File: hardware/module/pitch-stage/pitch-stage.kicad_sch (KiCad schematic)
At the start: 0 parts

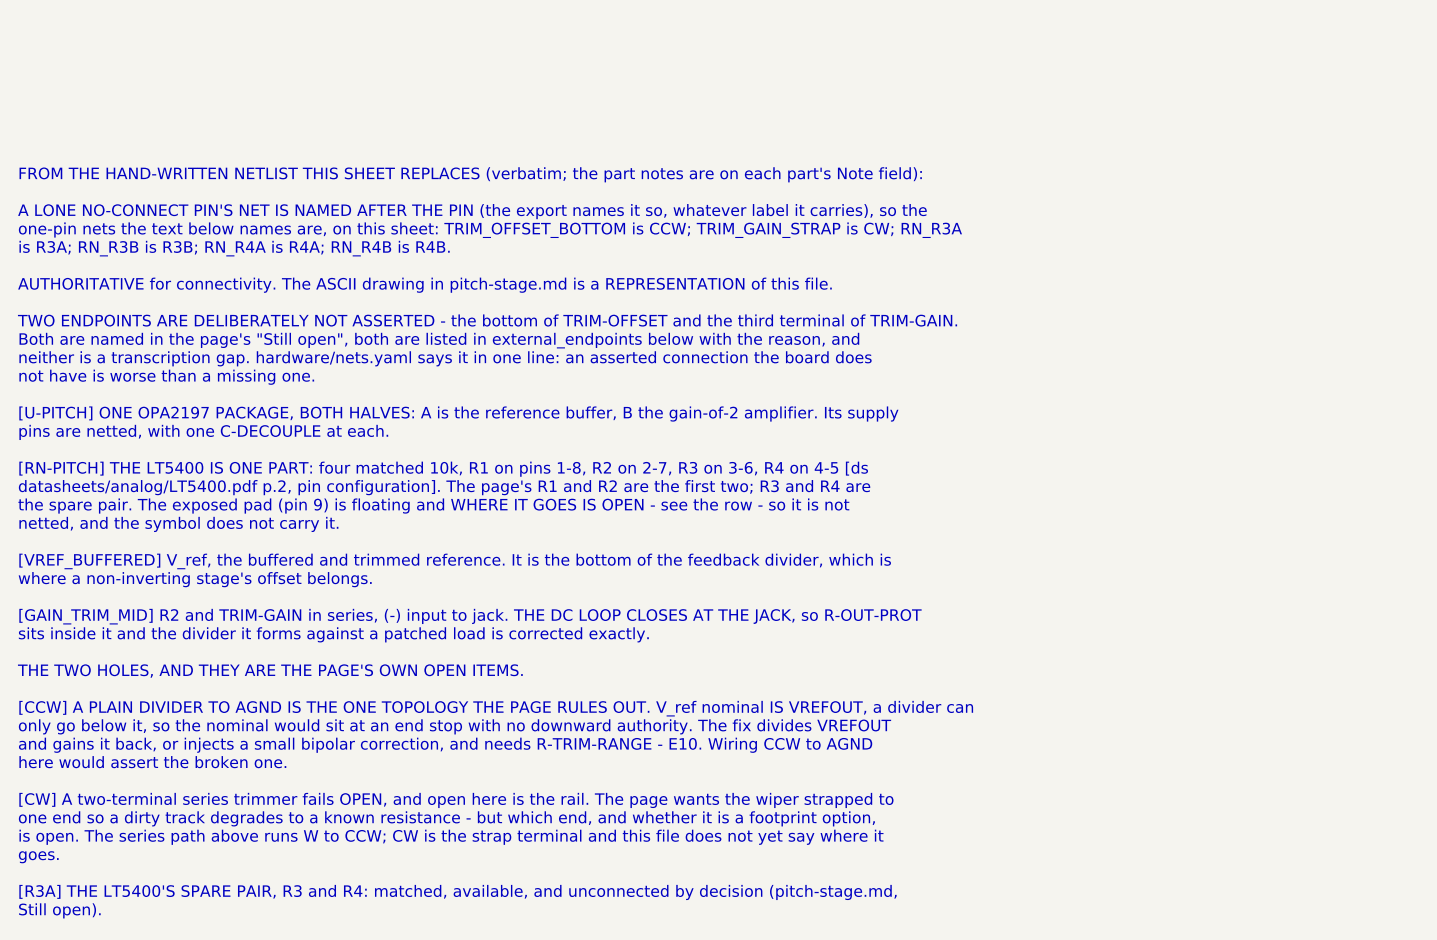
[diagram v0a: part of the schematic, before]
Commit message: Module: D3 turned round; pitch trims made buildable and bipolar; LT5400 pad and order code; breath-zero range resistor
D3 (the -12 V entry diode) was netlisted anode-to-bus, reverse-biased in
normal running (found by the analog sims): cathode to the bus now.
TRIM-OFFSET spans VREFOUT-AGND and injects through R-VREF-INJ against
R-VREF-SER into the follower at gain 1.02 (R-VREF-FB/R-VREF-GND): 2.500 V at
mid-travel, -60/+50 mV. It also holds the 3-state VREFOUT at 0 V while the
DAC's reference is disabled. TRIM-GAIN is centred by R-GAIN-CTR in the R1 leg
(+/-1 %) and its CW end strapped to the wiper. RN-PITCH carries its exposed
pad as pin 9 to AGND_MOD, spares tied down; ordered LT5400BIMS8E-1#PBF.
R-OPAMP-IN is six; R-TRIM-RANGE split into real parts. R-ZERO-TOP gives
TRIM-BREATH-ZERO the 0-1.0 V range its page specifies. Page text follows.

Co-Authored-By: Claude Opus 5.5 <noreply@anthropic.com>
Claude-Session: https://claude.ai/code/session_01LmB4muFXnoLprWX4JzuJ5A
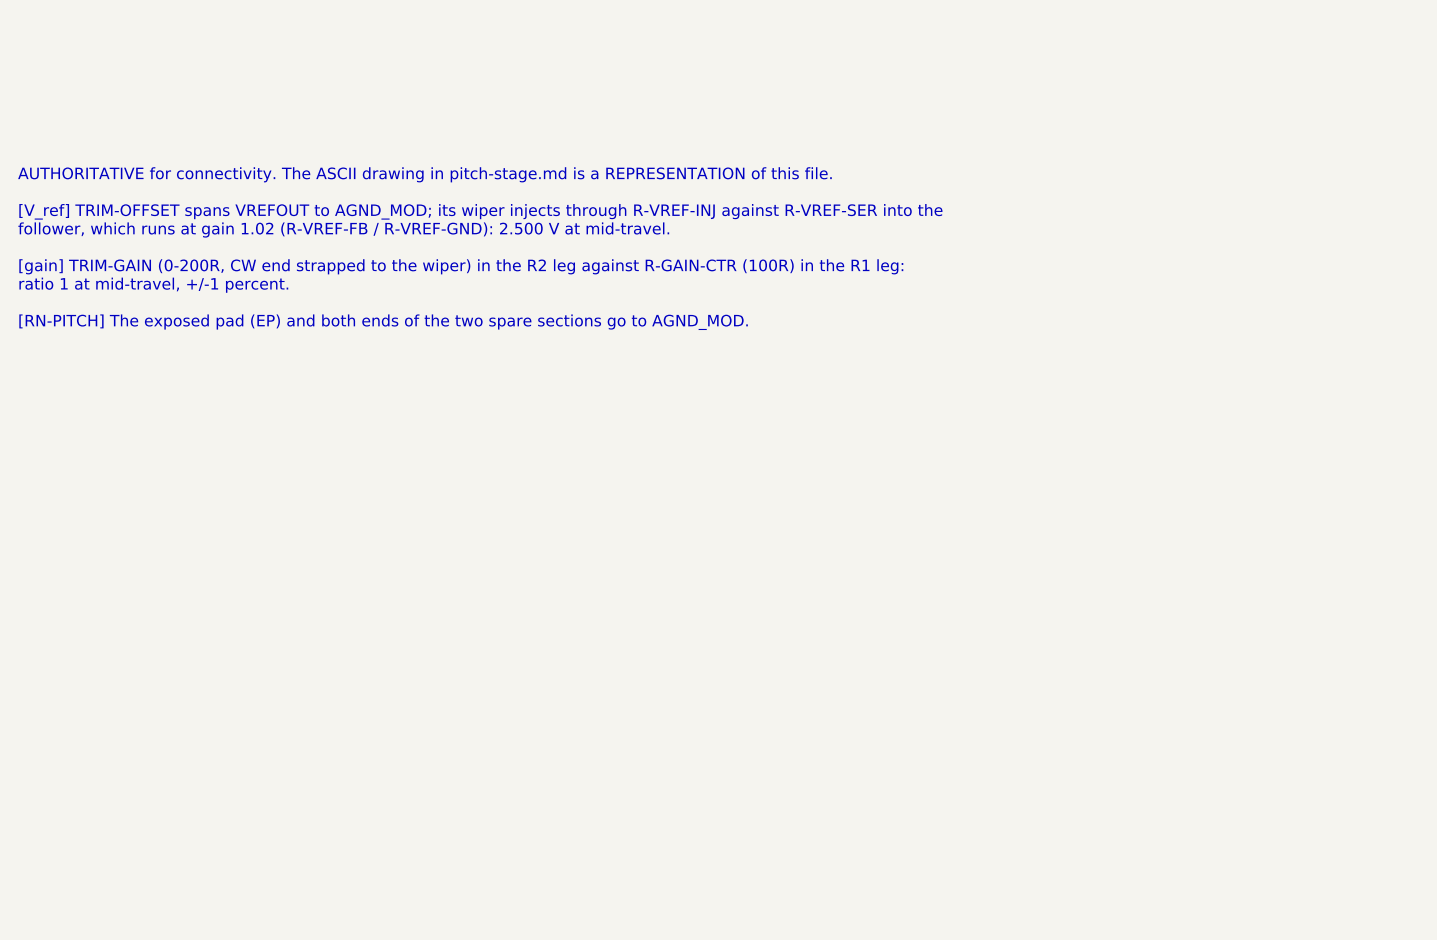
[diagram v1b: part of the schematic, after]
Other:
- note added: "AUTHORITATIVE for connectivity. The ASCII drawing in pitch-stage.md is a REPRESENTATION of this file. [V_ref] TRIM-OFFSET spans VREFOUT to AGND_MOD; its wiper injects through R-VREF-INJ against R-VREF-SER into the follower, which runs at gain 1.02 (R-VREF-FB / R-VREF-GND): 2.500 V at mid-travel. [gain] TRIM-GAIN (0-200R, CW end strapped to the wiper) in the R2 leg against R-GAIN-CTR (100R) in the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"
- note removed: "FROM THE HAND-WRITTEN NETLIST THIS SHEET REPLACES (verbatim; the part notes are on each part's Note field): A LONE NO-CONNECT PIN'S NET IS NAMED AFTER THE PIN (the export names it so, whatever label it carries), so the one-pin nets the text below names are, on this sheet: TRIM_OFFSET_BOTTOM is CCW; TRIM_GAIN_STRAP is CW; RN_R3A is R3A; RN_R3B is R3B; RN_R4A is R4A; RN_R4B is R4B. AUTHORITATIVE fo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"
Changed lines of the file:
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@@
     (property "From" "module/power-entry" (at 269.24 55.88 0) (effects (font (size 1.27 1.27)) hide))
     (property "Figure" "dig-gnd-topology" (at 269.24 55.88 0) (effects (font (size 1.27 1.27)) hide)))
-  (text "FROM THE HAND-WRITTEN NETLIST THIS SHEET REPLACES (verbatim; the part notes are on each part's Note field):\n\nA LONE NO-CONNECT PIN'S NET IS NAMED AFTER THE PIN (the export names it so, whatever label it carries), so the\none-pin nets the text below names are, on this sheet: TRIM_OFFSET_BOTTOM is CCW; TRIM_GAIN_STRAP is CW; RN_R3A\nis R3A; RN_R3B is R3B; RN_R4A is R4A; RN_R4B is R4B.\n\nAUTHORITATIVE for connectivity. The ASCII drawing in pitch-stage.md is a REPRESENTATION of this file.\n\nTWO ENDPOINTS ARE DELIBERATELY NOT ASSERTED - the bottom of TRIM-OFFSET and the third terminal of TRIM-GAIN.\nBoth are named in the page's \"Still open\", both are listed in external_endpoints below with the reason, and\nneither is a transcription gap. hardware/nets.yaml says it in one line: an asserted connection the board does\nnot have is worse than a missing one.\n\n[U-PITCH] ONE OPA2197 PACKAGE, BOTH HALVES: A is the reference buffer, B the gain-of-2 amplifier. Its supply\npins are netted, with one C-DECOUPLE at each.\n\n[RN-PITCH] THE LT5400 IS ONE PART: four matched 10k, R1 on pins 1-8, R2 on 2-7, R3 on 3-6, R4 on 4-5 [ds\ndatasheets/analog/LT5400.pdf p.2, pin configuration]. The page's R1 and R2 are the first two; R3 and R4 are\nthe spare pair. The exposed pad (pin 9) is floating and WHERE IT GOES IS OPEN - see the row - so it is not\nnetted, and the symbol does not carry it.\n\n[VREF_BUFFERED] V_ref, the buffered and trimmed reference. It is the bottom of the feedback divider, which is\nwhere a non-inverting stage's offset belongs.\n\n[GAIN_TRIM_MID] R2 and TRIM-GAIN in series, (-) input to jack. THE DC LOOP CLOSES AT THE JACK, so R-OUT-PROT\nsits inside it and the divider it forms against a patched load is corrected exactly.\n\nTHE TWO HOLES, AND THEY ARE THE PAGE'S OWN OPEN ITEMS.\n\n[CCW] A PLAIN DIVIDER TO AGND IS THE ONE TOPOLOGY THE PAGE RULES OUT. V_ref nominal IS VREFOUT, a divider can\nonly go below it, so the nominal would sit at an end stop with no downward authority. The fix divides VREFOUT\nand gains it back, or injects a small bipolar correction, and needs R-TRIM-RANGE - E10. Wiring CCW to AGND\nhere would assert the broken one.\n\n[CW] A two-terminal series trimmer fails OPEN, and open here is the rail. The page wants the wiper strapped to\none end so a dirty track degrades to a known resistance - but which end, and whether it is a footprint option,\nis open. The series path above runs W to CCW; CW is the strap terminal and this file does not yet say where it\ngoes.\n\n[R3A] THE LT5400'S SPARE PAIR, R3 and R4: matched, available, and unconnected by decision (pitch-stage.md,\nStill open)." (at 40.64 147.32 0) (effects (font (size 1.27 1.27)) (justify left top)))
+  (text "AUTHORITATIVE for connectivity. The ASCII drawing in pitch-stage.md is a REPRESENTATION of this file.\n\n[V_ref] TRIM-OFFSET spans VREFOUT to AGND_MOD; its wiper injects through R-VREF-INJ against R-VREF-SER into the\nfollower, which runs at gain 1.02 (R-VREF-FB / R-VREF-GND): 2.500 V at mid-travel.\n\n[gain] TRIM-GAIN (0-200R, CW end strapped to the wiper) in the R2 leg against R-GAIN-CTR (100R) in the R1 leg:\nratio 1 at mid-travel, +/-1 percent.\n\n[RN-PITCH] The exposed pad (EP) and both ends of the two spare sections go to AGND_MOD." (at 40.64 147.32 0) (effects (font (size 1.27 1.27)) (justify left top)))
   (text "THIS CIRCUIT IS ON BOTH MODULE BOARDS (ADR 0023). Page main holds its main-board parts, page jack the parts behind the panel; the labels here join the two pages, and on the boards J-B2B-MOD joins them. Each board places its own page." (at 60.96 30.48 0) (effects (font (size 1.27 1.27)) (justify left top)))
   (sheet_instances (path "/" (page "1")))
